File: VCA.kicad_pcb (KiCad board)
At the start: 2 copper layers, 39.6 x 100 mm, 84 parts, among them J1 AudioJack2_Ground_Switch, J2 AudioJack2_Ground_Switch, J3 AudioJack2_Ground_Switch, J4 AudioJack2_Ground_Switch, J5 AudioJack2_Ground_Switch, J6 AudioJack2_Ground_Switch, J7 Conn_02x05_Odd_Even, Q1 2N2222, Q2 2N2222, Q3 2N2907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

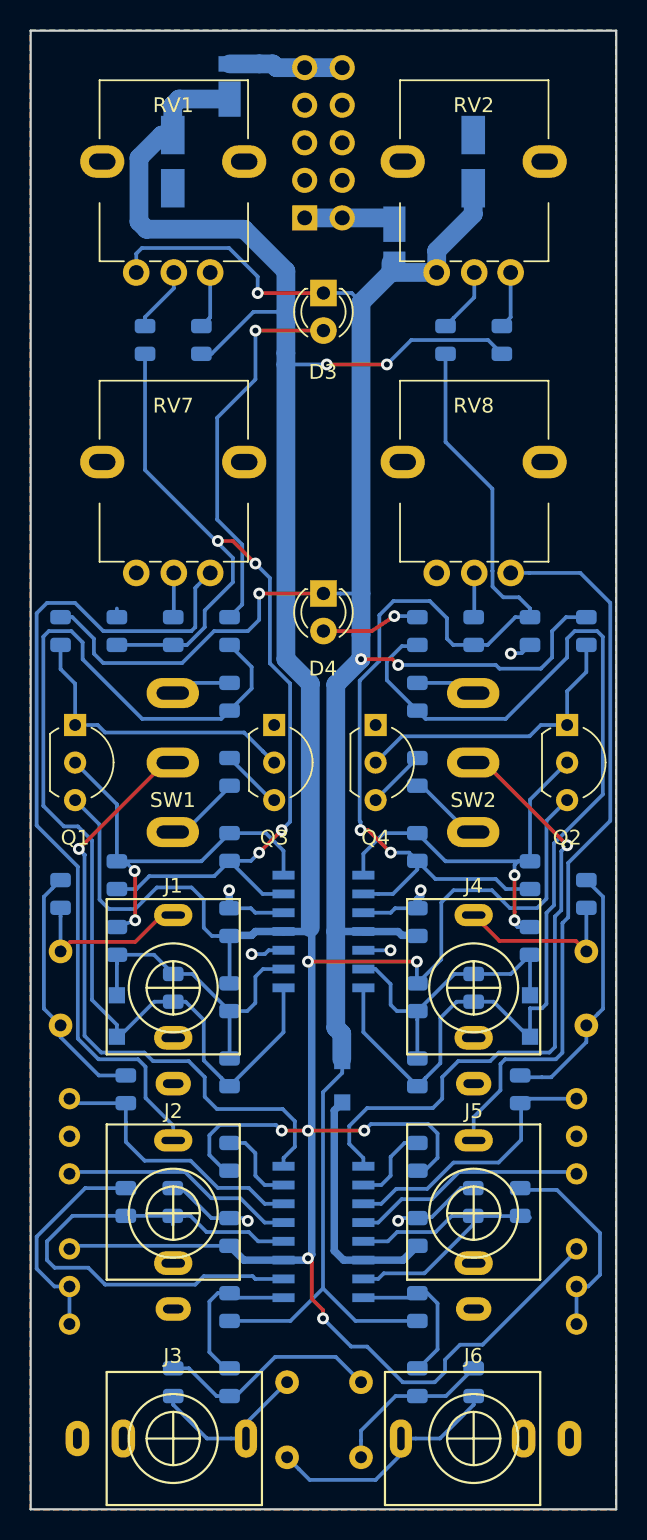
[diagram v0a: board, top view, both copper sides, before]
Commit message: Avoid traces outside pour.
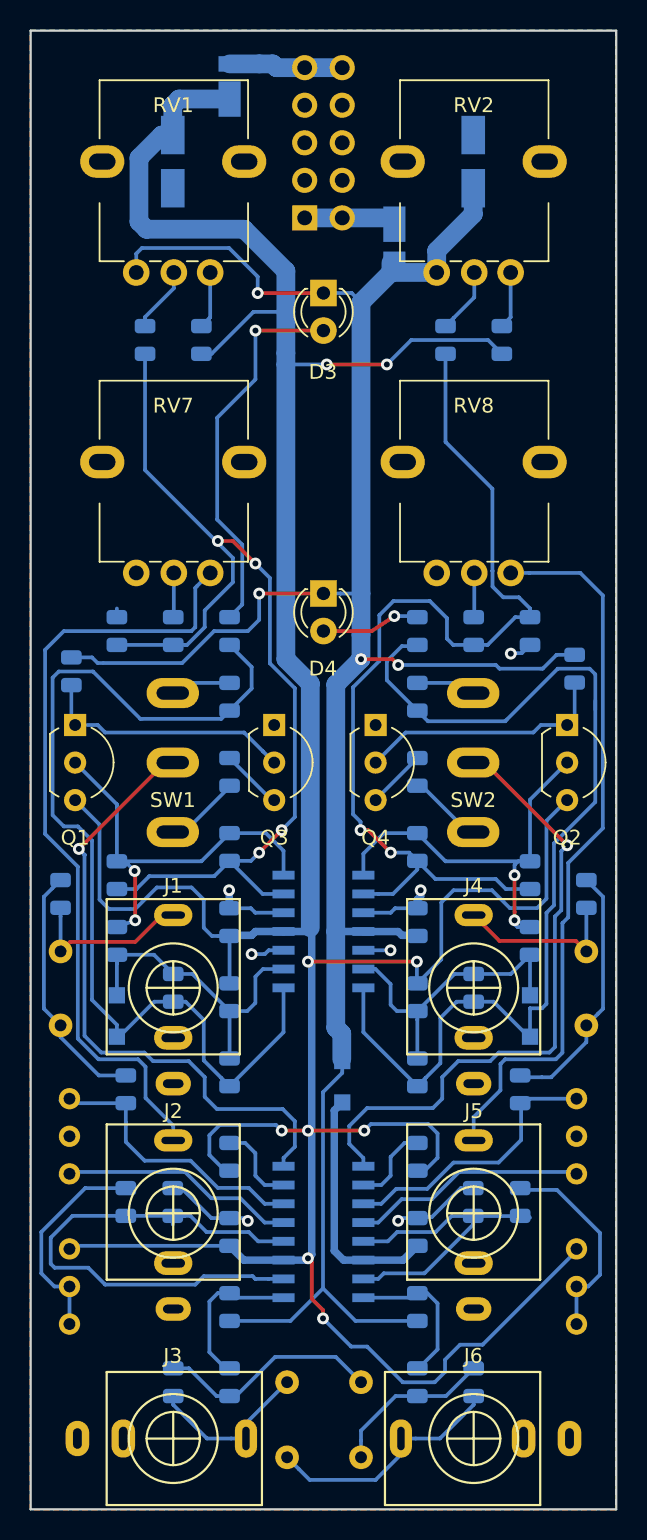
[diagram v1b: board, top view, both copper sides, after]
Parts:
- moved R21 2.82 mm to (110.0, 96.2)
- moved R22 2.67 mm to (144.0, 96.0)
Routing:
- net LEDA: track 72.2 -> 66.8 mm
- net -12V: track 163.7 -> 158.3 mm
- net LEDB: track 73.3 -> 69.2 mm
- net Net-(J2-PadT): track 57.0 -> 53.2 mm
- net Net-(Q1-Pad1): track 20.3 -> 17.3 mm
- net Net-(Q2-Pad1): track 20.0 -> 17.1 mm
